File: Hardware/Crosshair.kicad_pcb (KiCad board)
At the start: 4 copper layers, 57.4 x 40 mm, 165 parts, among them IC1 LTC4413EDD#PBF, J1 DM3AT-SF-PEJM5_40_, J2 USB_C_Receptacle_USB2.0, J3 XT30PW-M, J4 USB_C_Receptacle_USB2.0, J5 7788, J6 7788, Q1 SISS23DN-T1-GE3, Q2 BSZ025N04LS, Q3 BSZ025N04LS, Q4 BSZ025N04LS, Q5 SSM3K15AMFV,L3F, U1 ESP32-S3, U10 TPS55288QRPMRQ1, U11 DPS368, U12 TCMT1109, U2 SN65HVD230, U3 LM66200DRLR, U4 MAX77827AEFD+T, U5 SC4215ASTRT, Y1 R940000171

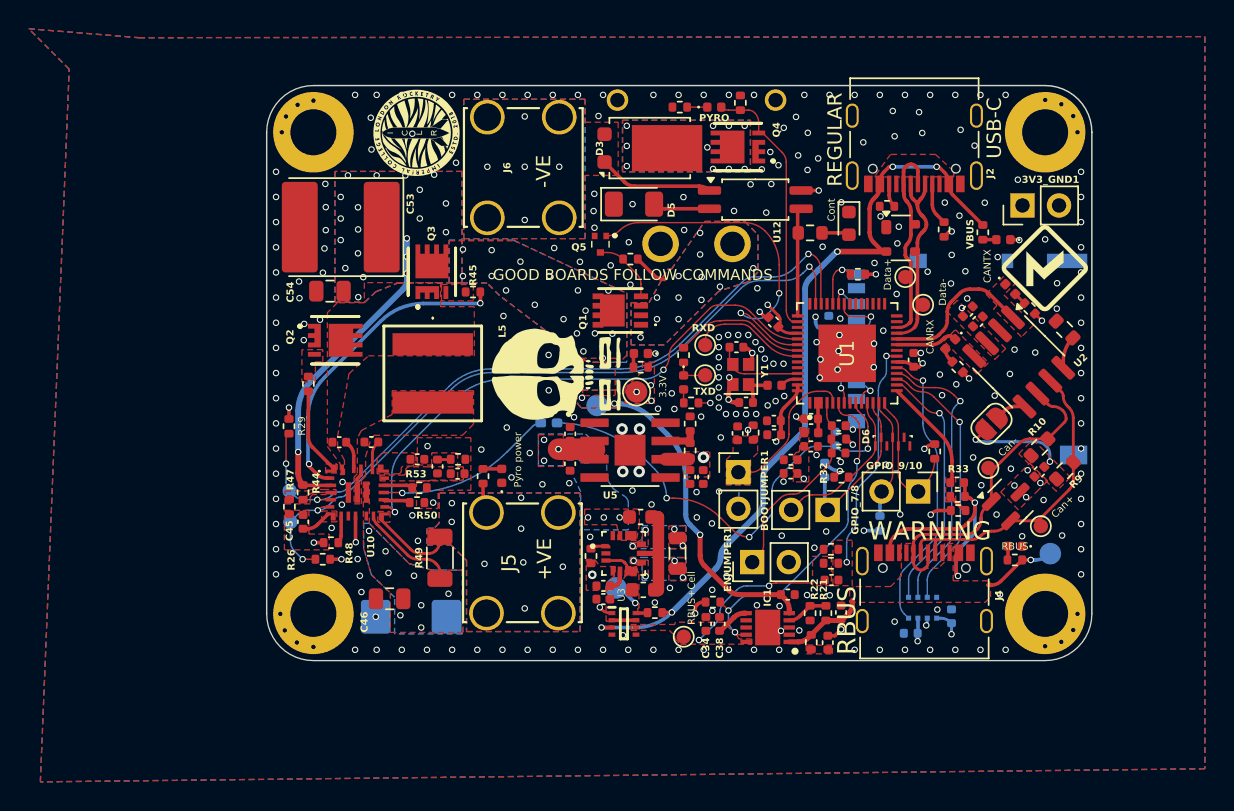
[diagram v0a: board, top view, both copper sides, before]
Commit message: changed 1 footprint
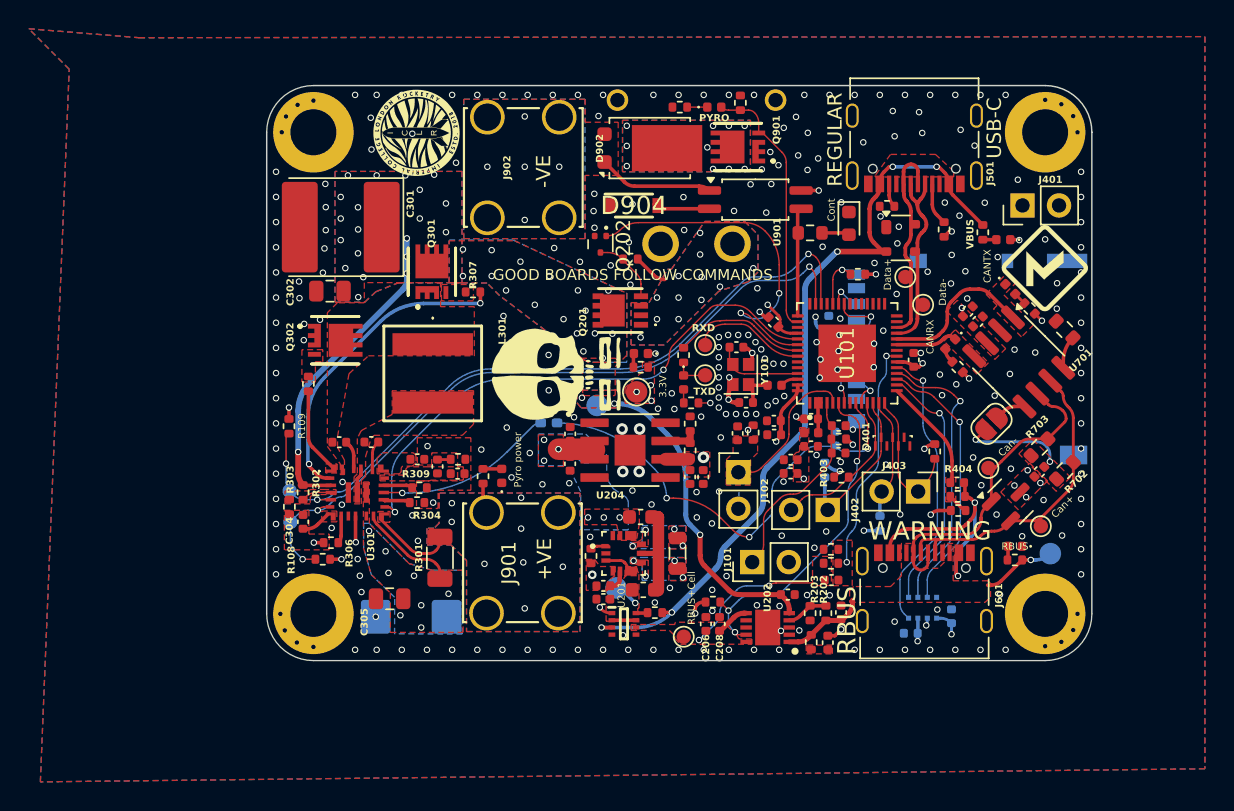
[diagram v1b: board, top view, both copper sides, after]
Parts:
- removed REF**: Symbol_Attention_Triangle_8x7mm_Copper, Symbol:Symbol_Attention_Triangle_8x7mm_Copper
- C1002: renamed from C37; value 0.1uF -> 100nF
- C103: renamed from C3; value 0.1uF -> 100nF
- C105: renamed from C5; value 0.1uF -> 100nF
- C106: renamed from C6; value 0.1uF -> 100nF
- C109: renamed from C8; value 0.1uF -> 100nF
- C110: renamed from C10; value 0.1uF -> 100nF
- C111: renamed from C11; value 0.1uF -> 100nF
- C203: renamed from C56; value 0.1uF -> 100nF
- C205: renamed from C57; value 0.1uF -> 100nF
- C215: renamed from C27; value 0.1uF -> 100nF
- C306: renamed from C52; value 0.1uF -> 100nF
- C307: renamed from C51; value 0.1uF -> 100nF
- C309: renamed from C49; value 1.2nf -> 1.2nF
- C311: renamed from C28; value 0.1uF -> 100nF
- D101: renamed from TXLED1; value GREEN_LED -> LED_GREEN
- D102: renamed from CTXLED1; value GREEN_LED -> LED_GREEN
- D103: renamed from CRXLED1; value ORANGE_LED -> LED_ORANGE
- D104: renamed from 3V3LED1; value BLUE_LED -> LED_BLUE
- D502: renamed from USBLED1; value WHITE_LED -> LED_WHITE
- D601: renamed from RBUSLED1; value WHITE_LED -> LED_WHITE
- D901: renamed from Firing1; value EMERALD_LED -> LED_GREEN
- D903: renamed from D4; value RED_LED -> LED_RED
- D904: renamed from D5; value 954-S-102T -> S-102T; footprint Diode_SMD:D_1206_3216Metric -> iclr:SODFL3516X70N
- L101: renamed from L1; value 2.0nH -> 2nH
- L301: renamed from L5; value PA5432472NLT -> 4.7uH
- LED301: renamed from LED5; value RED_LED -> LED_RED
- Q202: renamed from Q5; footprint iclr:SSM3K15AMFVL3F -> Package_TO_SOT_SMD:SOT-723
- R107: renamed from R6; value 499R -> 499Ω
- R401: renamed from R30; value 10k -> 10kΩ
- R402: renamed from R31; value 10k -> 10kΩ
- R403: renamed from R32; value 10k -> 10kΩ
- R404: renamed from R33; value 10k -> 10kΩ
- Y101: renamed from Y1; value R940000171 -> 40MHz±10ppm
- moved D904 0.10 mm to (113.8, 79.7)
- turned Q202 to -90 degrees
- renumbered C19 to C1001, C1 to C101, C2 to C102, C4 to C104, C7 to C107, C9 to C108, C13 to C112, C14 to C113, C35 to C201, C39 to C202, C36 to C204, C34 to C206, C20 to C207, C38 to C208, C21 to C209, C22 to C210, C23 to C211, C24 to C212, C25 to C213, C26 to C214, C53 to C301, C54 to C302, C47 to C303, C45 to C304, C46 to C305, C50 to C308, C48 to C310, C15 to C701, C16 to C702, C17 to C703, C12 to C801, C18 to C802, D6 to D401, D2 to D501, D1 to D701, D3 to D902, H1 to H101, H2 to H102, H3 to H103, H4 to H104, J1 to J1001, ENJUMPER1 to J101, BOOTJUMPER1 to J102, J3 to J201, 3V3_GND1 to J401, GPIO_7/8 to J402, GPIO_9/10 to J403, J2 to J501, J4 to J601, J5 to J901, J6 to J902, JP2 to JP301, JP1 to JP701, L2 to L102, L3 to L201, Q1 to Q201, Q3 to Q301, Q2 to Q302, Q4 to Q901, R35 to R1001, R1 to R101, R2 to R102, R5 to R103, R18 to R104, R3 to R105, R4 to R106, R26 to R108, R29 to R109, R37 to R201, R21 to R202, R22 to R203, R40 to R204, R41 to R205, R14 to R206, R23 to R207, R24 to R208, R27 to R209, R15 to R210, R36 to R211, R16 to R212, R17 to R213, R49 to R301, R44 to R302, R47 to R303, R50 to R304, R7 to R305, R48 to R306, R45 to R307, R46 to R308, R53 to R309, R52 to R310, R11 to R501, R12 to R502, R13 to R503, R25 to R601, R8 to R701, R9 to R702, R10 to R703, R39 to R901, R19 to R902, R20 to R903, TP9 to TP101, TP10 to TP102, TP12 to TP103, TP11 to TP104, TP13 to TP201, TP4 to TP202, TP5 to TP203, TP6 to TP204, TP14 to TP205, TP8 to TP206, TP1 to TP501, TP2 to TP502, TP3 to TP601, TP7 to TP602, U1 to U101, U3 to U201, IC1 to U202, U4 to U203, U5 to U204, U10 to U301, U2 to U701, U11 to U801, U12 to U901
